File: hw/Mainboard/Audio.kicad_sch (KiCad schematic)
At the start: 14 parts, among them J1 SJ-43504-SMT-TR, U22 LM386

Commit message: hw: wip
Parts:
- C30: LCSC C1525 -> C307331
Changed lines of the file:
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@@
       (effects (font (size 1.27 1.27)) hide)
     )
-    (property "Datasheet" "https://datasheet.lcsc.com/lcsc/1810191219_Samsung-Electro-Mechanics-CL05B104KO5NNNC_C1525.pdf" (id 3) (at 149.86 66.04 0)
+    (property "Datasheet" "" (id 3) (at 149.86 66.04 0)
       (effects (font (size 1.27 1.27)) hide)
     )
-    (property "LCSC" "C1525" (id 4) (at 149.86 66.04 0)
+    (property "LCSC" "C307331" (id 4) (at 149.86 66.04 0)
       (effects (font (size 1.27 1.27)) hide)
     )

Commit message: hw: wip
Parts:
- U22: MOUSER (none) -> 926-LM386N-1/NOPB
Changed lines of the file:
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@@
+      (effects (font (size 1.27 1.27)) hide)
+    )
+    (property "MOUSER" "926-LM386N-1/NOPB" (id 4) (at 167.64 73.66 0)
       (effects (font (size 1.27 1.27)) hide)
     )

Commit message: hw: wip
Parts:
- C55: footprint Capacitor_SMD:C_0402_1005Metric -> Capacitor_SMD:C_0603_1608Metric; LCSC C25118 -> C1622
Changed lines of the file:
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@@
       (effects (font (size 1.27 1.27)) hide)
     )
-    (property "Datasheet" "" (id 3) (at 149.86 66.04 0)
+    (property "Datasheet" "https://datasheet.lcsc.com/lcsc/2304140030_Samsung-Electro-Mechanics-CL05B104KB54PNC_C307331.pdf" (id 3) (at 149.86 66.04 0)
       (effects (font (size 1.27 1.27)) hide)
     )
@@
       (effects (font (size 1.27 1.27)) hide)
     )
-    (property "Datasheet" "~" (id 3) (at 87.63 96.52 0)
+    (property "Datasheet" "" (id 3) (at 87.63 96.52 0)
       (effects (font (size 1.27 1.27)) hide)
     )
@@
       (effects (font (size 1.27 1.27)) hide)
     )
-    (property "Datasheet" "~" (id 3) (at 87.63 88.9 0)
+    (property "Datasheet" "https://datasheet.lcsc.com/lcsc/2304140030_FH--Guangdong-Fenghua-Advanced-Tech-0402B223K500NT_C1532.pdf" (id 3) (at 87.63 88.9 0)
       (effects (font (size 1.27 1.27)) hide)
     )
@@
       (effects (font (size 1.27 1.27)) (justify left bottom) hide)
     )
-    (property "Datasheet" "https://www.mouser.com/datasheet/2/670/sj_43504_smt_tr-1779335.pdf" (id 3) (at 118.11 85.09 0)
+    (property "Datasheet" "" (id 3) (at 118.11 85.09 0)
       (effects (font (size 1.27 1.27)) (justify left bottom) hide)
     )
@@
       (effects (font (size 1.27 1.27)) hide)
     )
-    (property "Datasheet" "~" (id 3) (at 149.86 85.09 0)
+    (property "Datasheet" "" (id 3) (at 149.86 85.09 0)
       (effects (font (size 1.27 1.27)) hide)
     )
@@
       (effects (font (size 1.27 1.27)) hide)
     )
-    (property "Datasheet" "https://www.mouser.com/datasheet/2/334/AT-1220-TT-9-R-532252.pdf" (id 3) (at 209.296 74.93 0)
+    (property "Datasheet" "" (id 3) (at 209.296 74.93 0)
       (effects (font (size 1.27 1.27)) hide)
     )
@@
       (effects (font (size 1.27 1.27)) hide)
     )
-    (property "Datasheet" "~" (id 3) (at 157.48 62.23 0)
+    (property "Datasheet" "" (id 3) (at 157.48 62.23 0)
       (effects (font (size 1.27 1.27)) hide)
     )
@@
       (effects (font (size 1.27 1.27)) hide)
     )
-    (property "Datasheet" "http://www.ti.com/lit/ds/symlink/lm386.pdf" (id 3) (at 172.72 68.58 0)
+    (property "Datasheet" "" (id 3) (at 172.72 68.58 0)
       (effects (font (size 1.27 1.27)) hide)
     )
@@
       (effects (font (size 1.27 1.27)) hide)
     )
-    (property "Datasheet" "https://datasheet.lcsc.com/lcsc/1811091611_Samsung-Electro-Mechanics-CL05A105KA5NQNC_C52923.pdf" (id 3) (at 69.85 85.09 0)
+    (property "Datasheet" "https://datasheet.lcsc.com/lcsc/2304140030_Samsung-Electro-Mechanics-CL05A105KA5NQNC_C52923.pdf" (id 3) (at 69.85 85.09 0)
       (effects (font (size 1.27 1.27)) hide)
     )
@@
       (effects (font (size 1.27 1.27)) (justify left))
     )
-    (property "Footprint" "Capacitor_SMD:C_0402_1005Metric" (id 2) (at 181.61 80.01 0)
-      (effects (font (size 1.27 1.27)) hide)
-    )
-    (property "Datasheet" "~" (id 3) (at 181.61 80.01 0)
-      (effects (font (size 1.27 1.27)) hide)
-    )
-    (property "LCSC" "C25118" (id 4) (at 181.61 80.01 0)
+    (property "Footprint" "Capacitor_SMD:C_0603_1608Metric" (id 2) (at 181.61 80.01 0)
+      (effects (font (size 1.27 1.27)) hide)
+    )
+    (property "Datasheet" "https://datasheet.lcsc.com/lcsc/2304140030_Samsung-Electro-Mechanics-CL10B473KB8NNNC_C1622.pdf" (id 3) (at 181.61 80.01 0)
+      (effects (font (size 1.27 1.27)) hide)
+    )
+    (property "LCSC" "C1622" (id 4) (at 181.61 80.01 0)
       (effects (font (size 1.27 1.27)) hide)
     )
@@
       (effects (font (size 1.27 1.27)) hide)
     )
-    (property "Datasheet" "https://datasheet.lcsc.com/lcsc/1810221121_Samsung-Electro-Mechanics-CL31A476MPHNNNE_C96123.pdf" (id 3) (at 194.31 73.66 0)
-      (effects (font (size 1.27 1.27)) hide)
-    )
+    (property "Datasheet" "" (id 3) (at 194.31 73.66 0)
+      (effects (font (size 1.27 1.27)) hide)
+    )

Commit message: wip
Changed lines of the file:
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@@
       (effects (font (size 1.27 1.27)) (justify left bottom) hide)
     )
-    (property "Datasheet" "" (id 3) (at 118.11 85.09 0)
+    (property "Datasheet" "https://www.mouser.com/datasheet/2/670/sj_43504_smt_tr-1779335.pdf" (id 3) (at 118.11 85.09 0)
       (effects (font (size 1.27 1.27)) (justify left bottom) hide)
     )
@@
   (symbol (lib_id "Device:C_Small") (at 194.31 73.66 90) (unit 1)
     (in_bom yes) (on_board yes)
-    (property "Reference" "C54" (id 0) (at 194.31 67.31 90)
+    (property "Reference" "C54" (id 0) (at 195.58 67.31 90)
       (effects (font (size 1.27 1.27)) (justify left))
     )
@@
       (effects (font (size 1.27 1.27)) hide)
     )
-    (property "Datasheet" "" (id 3) (at 194.31 73.66 0)
+    (property "Datasheet" "https://datasheet.lcsc.com/lcsc/2304140030_Samsung-Electro-Mechanics-CL31A476MPHNNNE_C96123.pdf" (id 3) (at 194.31 73.66 0)
       (effects (font (size 1.27 1.27)) hide)
     )

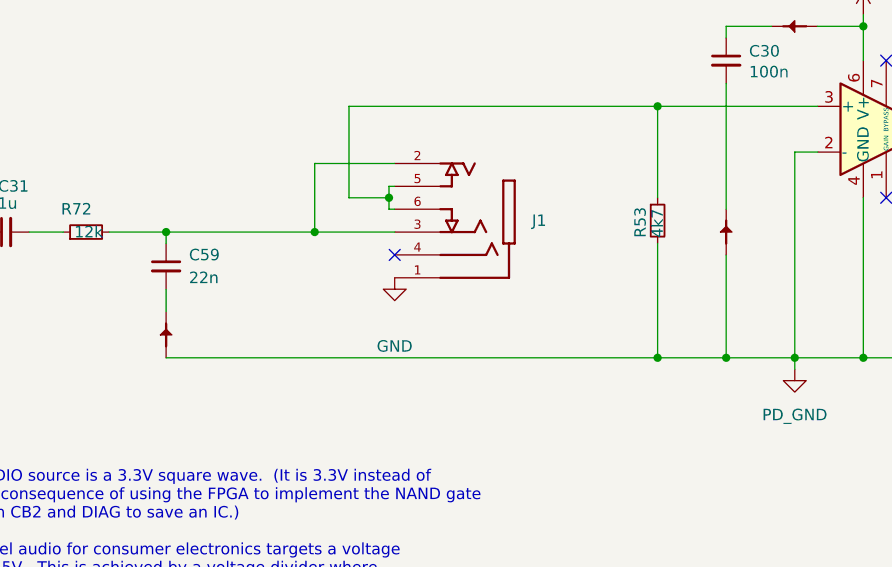
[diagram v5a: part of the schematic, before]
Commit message: hw: stitched copper planes (wip)
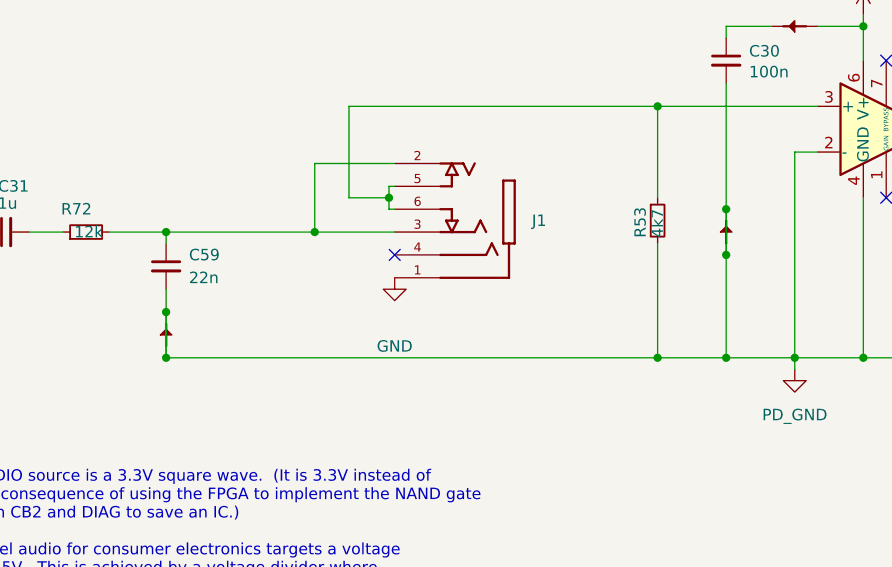
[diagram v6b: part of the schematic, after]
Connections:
- net PD_GND: now also C30.2, C59.2, PT36.2, PT38.2
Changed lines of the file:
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@@
     (title "CBM PET Mainboard Replacement")
   )
+  (junction (at 87.63 93.98) (diameter 0) (color 0 0 0 0)
+  )
   (junction (at 157.48 99.06) (diameter 0) (color 0 0 0 0)
+  )
+  (junction (at 149.86 82.55) (diameter 0) (color 0 0 0 0)
   )
   (junction (at 142.24 99.06) (diameter 0) (color 0 0 0 0)
@@
   (junction (at 165.1 62.23) (diameter 0) (color 0 0 0 0)
   )
+  (junction (at 87.63 99.06) (diameter 0) (color 0 0 0 0)
+  )
   (junction (at 142.24 71.12) (diameter 0) (color 0 0 0 0)
   )
@@
   )
   (junction (at 181.61 73.66) (diameter 0) (color 0 0 0 0)
+  )
+  (junction (at 149.86 87.63) (diameter 0) (color 0 0 0 0)
   )
   (junction (at 104.14 85.09) (diameter 0) (color 0 0 0 0)
@@
     (stroke (width 0) (type default) (color 0 0 0 0))
   )
+  (wire (pts (xy 87.63 93.98) (xy 87.63 99.06))
+    (stroke (width 0) (type default) (color 0 0 0 0))
+  )
   (wire (pts (xy 181.61 99.06) (xy 204.47 99.06))
     (stroke (width 0) (type default) (color 0 0 0 0))
   )
+  (wire (pts (xy 149.86 82.55) (xy 149.86 87.63))
+    (stroke (width 0) (type default) (color 0 0 0 0))
+  )

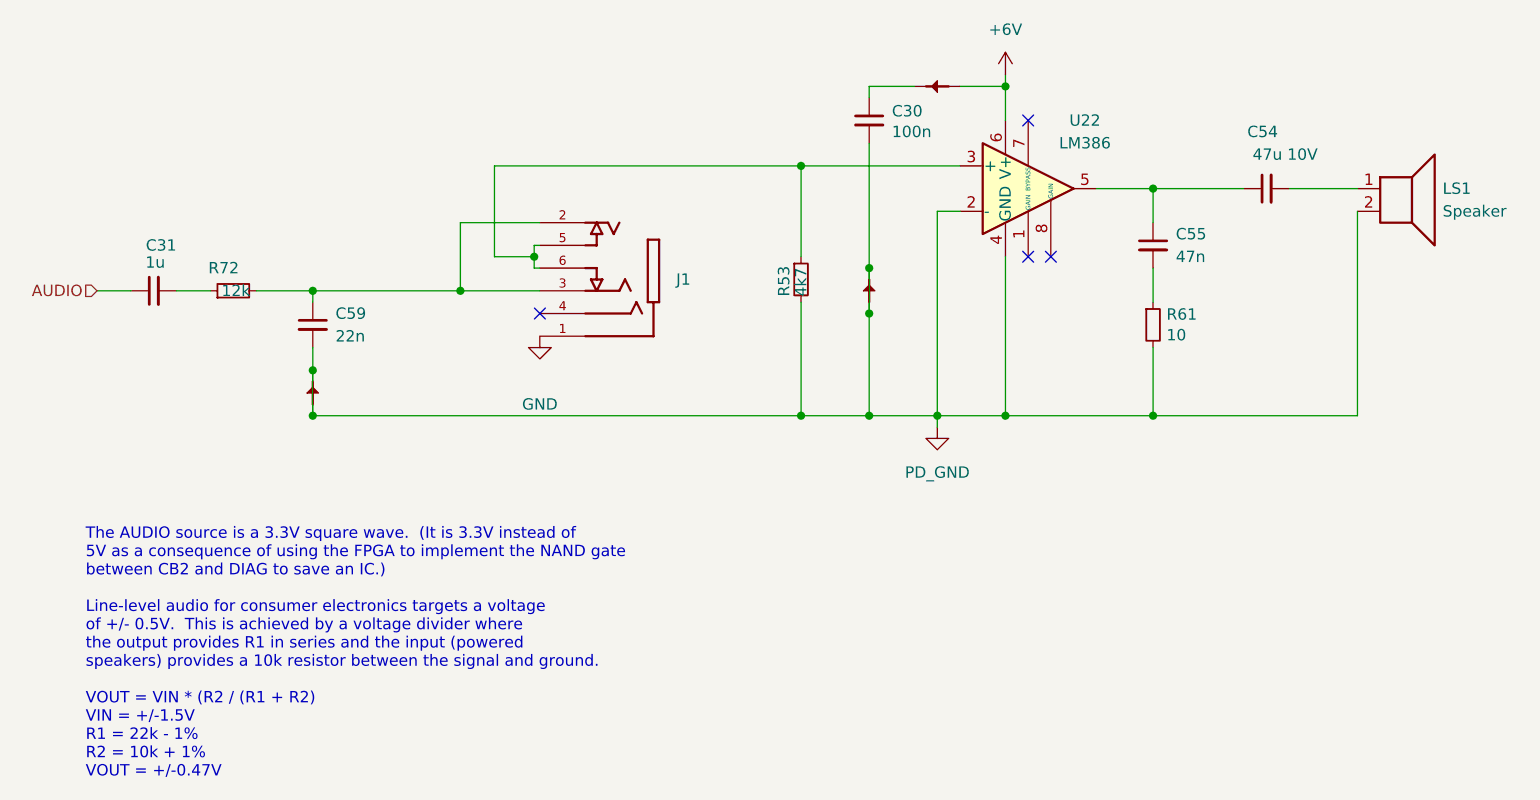
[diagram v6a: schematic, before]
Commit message: hw: 9V DC plug on left edge, change default track size
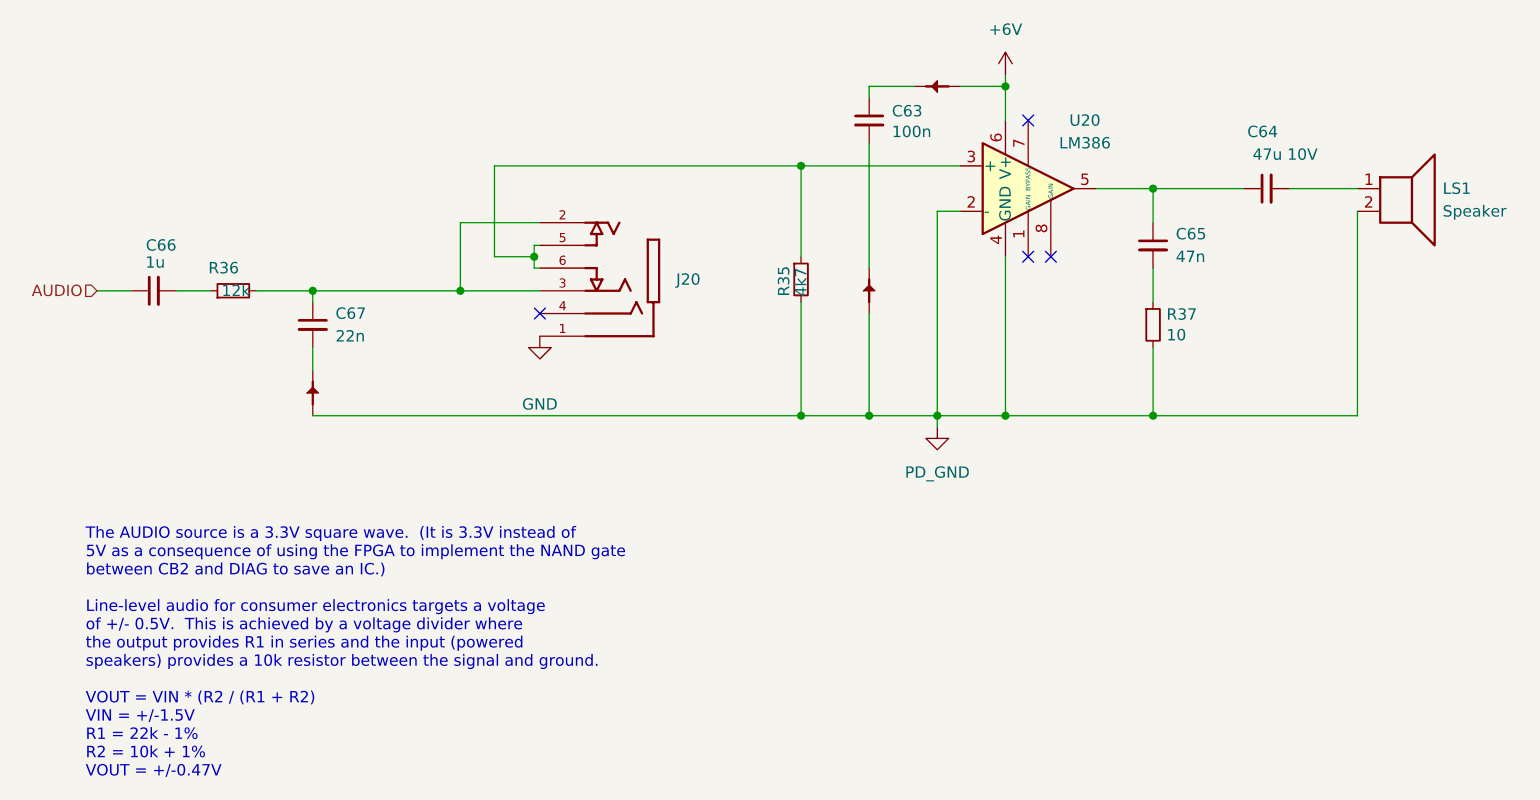
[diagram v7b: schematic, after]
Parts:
- renumbered C30 to C63, C54 to C64, C55 to C65, C31 to C66, C59 to C67, J1 to J20, PT35 to PT44, PT36 to PT45, PT38 to PT46, R53 to R35, R72 to R36, R61 to R37, U22 to U20
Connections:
- net PD_GND: no longer C63.2, C67.2, PT45.2, PT46.2
- new net: C63.2, PT45.2
- new net: C67.2, PT46.2
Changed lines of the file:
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@@
     (title "CBM PET Mainboard Replacement")
   )
-  (junction (at 87.63 93.98) (diameter 0) (color 0 0 0 0)
-  )
   (junction (at 157.48 99.06) (diameter 0) (color 0 0 0 0)
   )
-  (junction (at 149.86 82.55) (diameter 0) (color 0 0 0 0)
-  )
   (junction (at 142.24 99.06) (diameter 0) (color 0 0 0 0)
   )
@@
   (junction (at 165.1 62.23) (diameter 0) (color 0 0 0 0)
   )
-  (junction (at 87.63 99.06) (diameter 0) (color 0 0 0 0)
-  )
   (junction (at 142.24 71.12) (diameter 0) (color 0 0 0 0)
   )
@@
   )
   (junction (at 181.61 73.66) (diameter 0) (color 0 0 0 0)
-  )
-  (junction (at 149.86 87.63) (diameter 0) (color 0 0 0 0)
   )
   (junction (at 104.14 85.09) (diameter 0) (color 0 0 0 0)
@@
     (stroke (width 0) (type default) (color 0 0 0 0))
   )
-  (wire (pts (xy 87.63 93.98) (xy 87.63 99.06))
-    (stroke (width 0) (type default) (color 0 0 0 0))
-  )
   (wire (pts (xy 181.61 99.06) (xy 204.47 99.06))
-    (stroke (width 0) (type default) (color 0 0 0 0))
-  )
-  (wire (pts (xy 149.86 82.55) (xy 149.86 87.63))
     (stroke (width 0) (type default) (color 0 0 0 0))
   )
@@
   (symbol (lib_id "Device:R_Small") (at 78.74 85.09 90) (unit 1)
     (in_bom yes) (on_board yes)
-    (property "Reference" "R72" (id 0) (at 79.375 82.55 90)
+    (property "Reference" "R36" (id 0) (at 79.375 82.55 90)
       (effects (font (size 1.27 1.27)) (justify left))
     )
@@
   (symbol (lib_id "Device:C_Small") (at 149.86 66.04 0) (unit 1)
     (in_bom yes) (on_board yes)
-    (property "Reference" "C30" (id 0) (at 152.4 64.9986 0)
+    (property "Reference" "C63" (id 0) (at 152.4 64.9986 0)
       (effects (font (size 1.27 1.27)) (justify left))
     )
@@
   (symbol (lib_id "PET:PowerTie_2") (at 87.63 96.52 90) (unit 1)
     (in_bom yes) (on_board yes) (fields_autoplaced)
-    (property "Reference" "PT38" (id 0) (at 85.725 96.52 0)
+    (property "Reference" "PT46" (id 0) (at 85.725 96.52 0)
       (effects (font (size 1.27 1.27)) hide)
     )
@@
   (symbol (lib_id "power:GND") (at 113.03 90.17 0) (unit 1)
     (in_bom yes) (on_board yes)
-    (property "Reference" "#PWR0137" (id 0) (at 113.03 96.52 0)
+    (property "Reference" "#PWR0121" (id 0) (at 113.03 96.52 0)
       (effects (font (size 1.27 1.27)) hide)
     )
@@
   (symbol (lib_id "PET:PD_GND") (at 157.48 100.33 0) (unit 1)
     (in_bom yes) (on_board yes) (fields_autoplaced)
-    (property "Reference" "#PWR0136" (id 0) (at 157.48 106.68 0)
+    (property "Reference" "#PWR0122" (id 0) (at 157.48 106.68 0)
       (effects (font (size 1.27 1.27)) hide)
     )
@@
   (symbol (lib_id "power:+6V") (at 165.1 60.96 0) (unit 1)
     (in_bom yes) (on_board yes) (fields_autoplaced)
-    (property "Reference" "#PWR0126" (id 0) (at 165.1 64.77 0)
+    (property "Reference" "#PWR0120" (id 0) (at 165.1 64.77 0)
       (effects (font (size 1.27 1.27)) hide)
     )
@@
   (symbol (lib_id "Device:R_Small") (at 181.61 88.9 0) (unit 1)
     (in_bom yes) (on_board yes)
-    (property "Reference" "R61" (id 0) (at 183.1086 87.7316 0)
+    (property "Reference" "R37" (id 0) (at 183.1086 87.7316 0)
       (effects (font (size 1.27 1.27)) (justify left))
     )
@@
   (symbol (lib_id "Device:C_Small") (at 87.63 88.9 0) (unit 1)
     (in_bom yes) (on_board yes) (fields_autoplaced)
-    (property "Reference" "C59" (id 0) (at 90.17 87.6362 0)
+    (property "Reference" "C67" (id 0) (at 90.17 87.6362 0)
       (effects (font (size 1.27 1.27)) (justify left))
     )
@@
   (symbol (lib_id "SnapEDA:SJ-43504-SMT-TR") (at 118.11 85.09 180) (unit 1)
     (in_bom yes) (on_board yes) (fields_autoplaced)
-    (property "Reference" "J1" (id 0) (at 128.27 83.8199 0)
+    (property "Reference" "J20" (id 0) (at 128.27 83.8199 0)
       (effects (font (size 1.27 1.27)) (justify right))
     )
@@
   (symbol (lib_id "PET:PowerTie_2") (at 149.86 85.09 90) (unit 1)
     (in_bom yes) (on_board yes) (fields_autoplaced)
-    (property "Reference" "PT36" (id 0) (at 147.955 85.09 0)
+    (property "Reference" "PT45" (id 0) (at 147.955 85.09 0)
       (effects (font (size 1.27 1.27)) hide)
     )
@@
   (symbol (lib_id "PET:PowerTie_2") (at 157.48 62.23 180) (unit 1)
     (in_bom yes) (on_board yes) (fields_autoplaced)
-    (property "Reference" "PT35" (id 0) (at 157.48 64.135 0)
+    (property "Reference" "PT44" (id 0) (at 157.48 64.135 0)
       (effects (font (size 1.27 1.27)) hide)
     )
@@
   (symbol (lib_id "Amplifier_Audio:LM386") (at 167.64 73.66 0) (unit 1)
     (in_bom yes) (on_board yes)
-    (property "Reference" "U22" (id 0) (at 173.99 66.04 0))
+    (property "Reference" "U20" (id 0) (at 173.99 66.04 0))
     (property "Value" "LM386" (id 1) (at 173.99 68.58 0))
     (property "Footprint" "Package_DIP:DIP-8_W7.62mm" (id 2) (at 170.18 71.12 0)
@@
   (symbol (lib_id "Device:R_Small") (at 142.24 83.82 0) (unit 1)
     (in_bom yes) (on_board yes)
-    (property "Reference" "R53" (id 0) (at 140.335 85.725 90)
+    (property "Reference" "R35" (id 0) (at 140.335 85.725 90)
       (effects (font (size 1.27 1.27)) (justify left))
     )
@@
   (symbol (lib_id "Device:C_Small") (at 69.85 85.09 90) (unit 1)
     (in_bom yes) (on_board yes)
-    (property "Reference" "C31" (id 0) (at 72.39 80.01 90)
+    (property "Reference" "C66" (id 0) (at 72.39 80.01 90)
       (effects (font (size 1.27 1.27)) (justify left))
     )
@@
   (symbol (lib_id "Device:C_Small") (at 181.61 80.01 0) (unit 1)
     (in_bom yes) (on_board yes) (fields_autoplaced)
-    (property "Reference" "C55" (id 0) (at 184.15 78.7462 0)
+    (property "Reference" "C65" (id 0) (at 184.15 78.7462 0)
       (effects (font (size 1.27 1.27)) (justify left))
     )
@@
   (symbol (lib_id "Device:C_Small") (at 194.31 73.66 90) (unit 1)
     (in_bom yes) (on_board yes)
-    (property "Reference" "C54" (id 0) (at 195.58 67.31 90)
-      (effects (font (size 1.27 1.27)) (justify left))
-    )
+    (property "Reference" "C64" (id 0) (at 195.58 67.31 90)
+      (effects (font (size 1.27 1.27)) (justify left))
+    )

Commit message: hw: 25x2 header (wip)
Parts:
- renumbered J20 to J21
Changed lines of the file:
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@@
   (symbol (lib_id "power:GND") (at 113.03 90.17 0) (unit 1)
     (in_bom yes) (on_board yes)
-    (property "Reference" "#PWR0121" (id 0) (at 113.03 96.52 0)
+    (property "Reference" "#PWR0123" (id 0) (at 113.03 96.52 0)
       (effects (font (size 1.27 1.27)) hide)
     )
@@
   (symbol (lib_id "PET:PD_GND") (at 157.48 100.33 0) (unit 1)
     (in_bom yes) (on_board yes) (fields_autoplaced)
-    (property "Reference" "#PWR0122" (id 0) (at 157.48 106.68 0)
+    (property "Reference" "#PWR0124" (id 0) (at 157.48 106.68 0)
       (effects (font (size 1.27 1.27)) hide)
     )
@@
   (symbol (lib_id "power:+6V") (at 165.1 60.96 0) (unit 1)
     (in_bom yes) (on_board yes) (fields_autoplaced)
-    (property "Reference" "#PWR0120" (id 0) (at 165.1 64.77 0)
+    (property "Reference" "#PWR0122" (id 0) (at 165.1 64.77 0)
       (effects (font (size 1.27 1.27)) hide)
     )
@@
   (symbol (lib_id "SnapEDA:SJ-43504-SMT-TR") (at 118.11 85.09 180) (unit 1)
     (in_bom yes) (on_board yes) (fields_autoplaced)
-    (property "Reference" "J20" (id 0) (at 128.27 83.8199 0)
+    (property "Reference" "J21" (id 0) (at 128.27 83.8199 0)
       (effects (font (size 1.27 1.27)) (justify right))
     )
